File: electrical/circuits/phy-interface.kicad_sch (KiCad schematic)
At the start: 35 parts, among them J1 RJ45, U1 DP83848C, X1 ECS-2520MVQ-500-BN

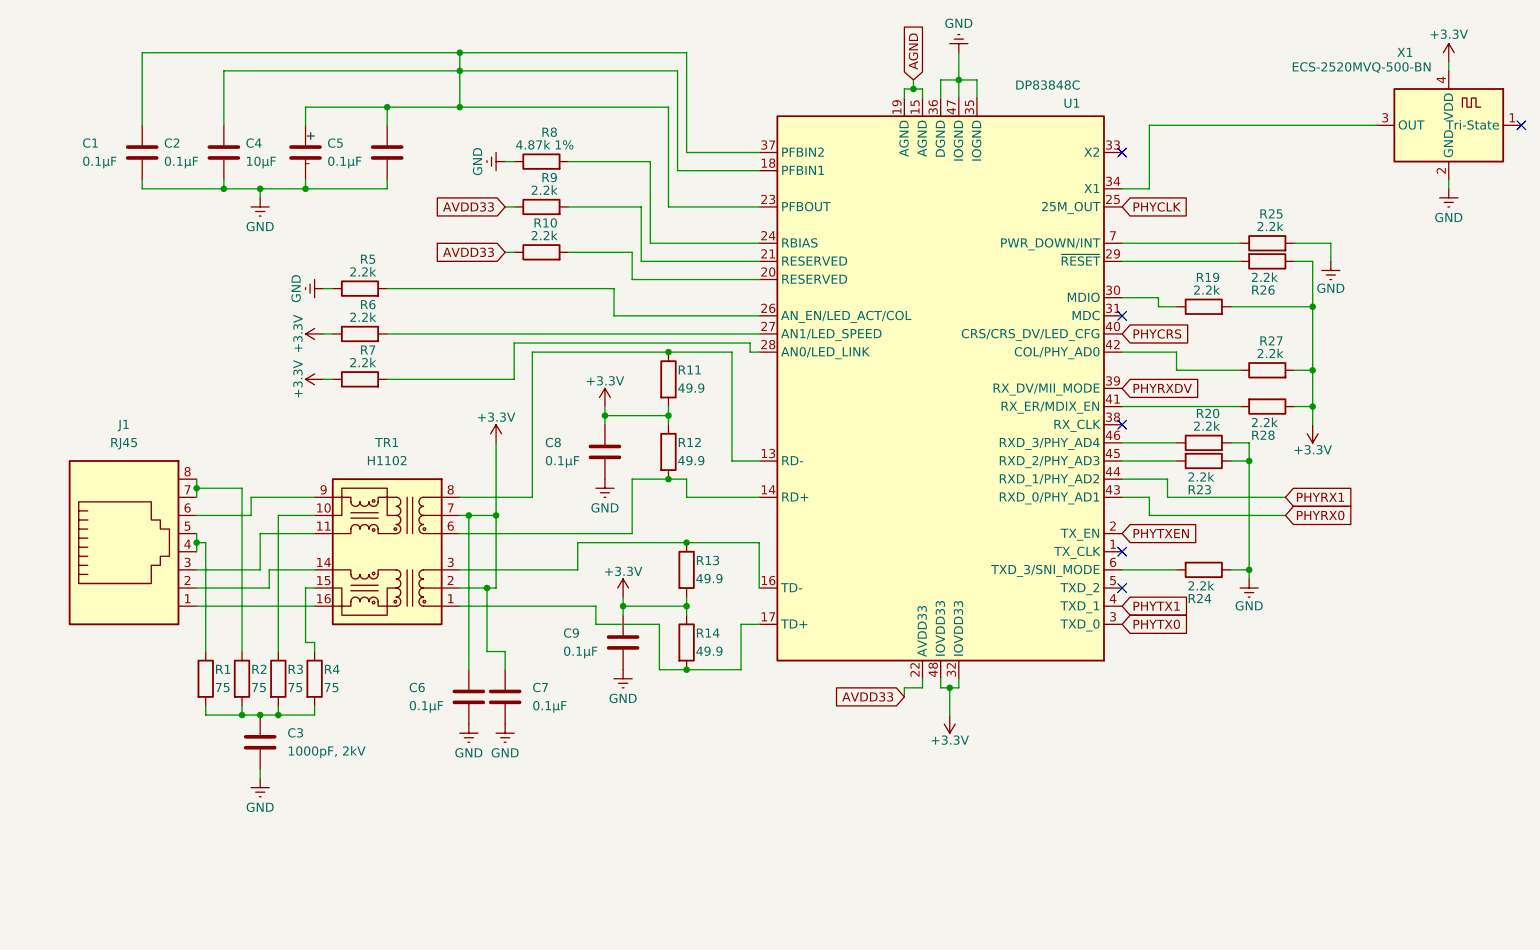
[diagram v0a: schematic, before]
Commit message: Updated circuit schematics for 10BASE-T SNI mode
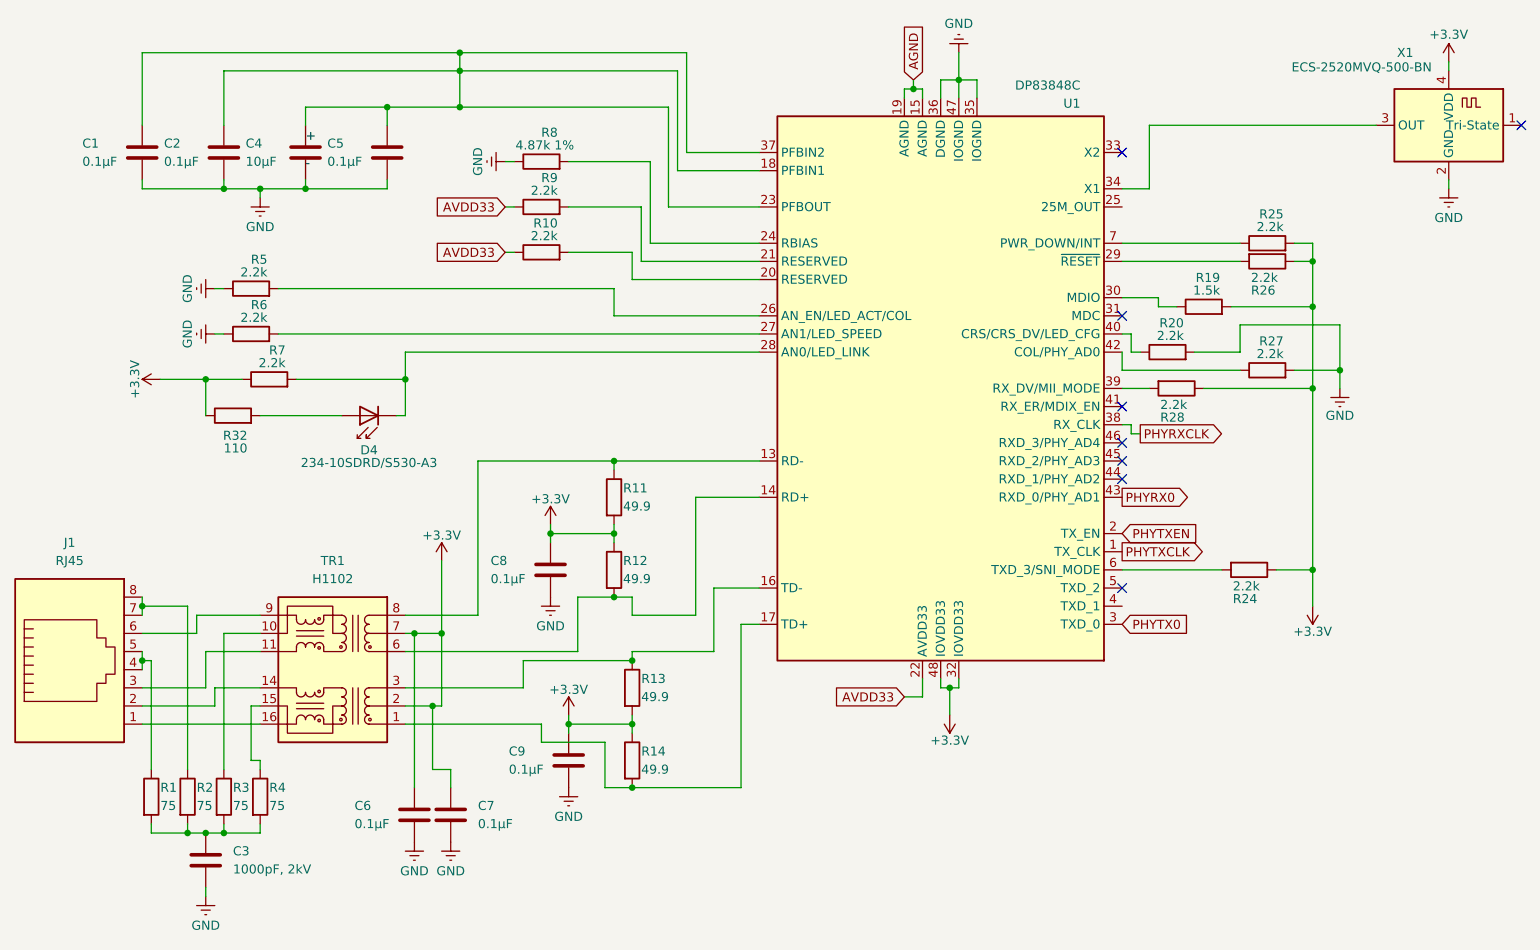
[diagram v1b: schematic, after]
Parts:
- removed R23: 2.2k, symbol Device:R
- added D4: 234-10SDRD/S530-A3, LED_THT:LED_D3.0mm_IRBlack, symbol LED:IR204A
- added R32: 110, symbol Device:R
- R19: value 2.2k -> 1.5k
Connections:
- net PHYCRS is gone; now on an unnamed net: U1.40 (CRS/CRS_DV/LED_CFG)
- net PHYRXDV is gone; now on an unnamed net: U1.39 (RX_DV/MII_MODE)
- net +3.3V: now also R24.1, R25.2, R32.1; no longer R27.2, R6.1
- net GND: now also R27.2, R6.1; no longer R24.1, R25.2
- net at R7.2, U1.28 (AN0/LED_LINK): now also D4.1 (K)
- net at R20.1: no longer U1.46 (RXD_3/PHY_AD4)
- net PHYTXCLK: now reaches U1.1 (TX_CLK)
- net PHYRXCLK: now reaches U1.38 (RX_CLK)
- net at R28.2: no longer U1.41 (RX_ER/MDIX_EN)
- net PHYCLK: no longer names the net of U1.25 (25M_OUT)
- net PHYRX1: no longer names the net of U1.44 (RXD_1/PHY_AD2)
- net PHYTX1: no longer names the net of U1.4 (TXD_1)
- new net: D4.2 (A), R32.2
- no-connect marks 6 -> 8
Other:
- title: (none) -> Free Space Optical 10BASE-T Ethernet Transceiver Circuit
- moved on the sheet: C3, C6, C7, C8, C9, J1, R1, R11, R12, R13, R14, R2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
